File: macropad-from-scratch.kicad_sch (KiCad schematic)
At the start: 0 parts

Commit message: added the MCU, some resistors, and a capacitor
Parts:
- added C1: 1uF, symbol Device:C_Small
- added R1: 10k, symbol Device:R_Small
- added R2, R3: 22, symbol Device:R_Small
- added U3: ATmega32U4-A, Package_QFP:TQFP-44_10x10mm_P0.8mm, symbol MCU_Microchip_ATmega:ATmega32U4-A
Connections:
- new net: R3.2, U3.3 (D-)
- new net: R1.1, U3.33 (~{HWB}/PE2)
- new net: R2.2, U3.4 (D+)
- new net: C1.1, U3.6 (UCAP)
- new net +5V: U3.14 (VCC), U3.2 (UVCC), U3.24 (AVCC), U3.34 (VCC), U3.44 (AVCC)
- new net GND: R1.2, U3.15 (GND), U3.23 (GND), U3.35 (GND), U3.43 (GND), U3.5 (UGND)

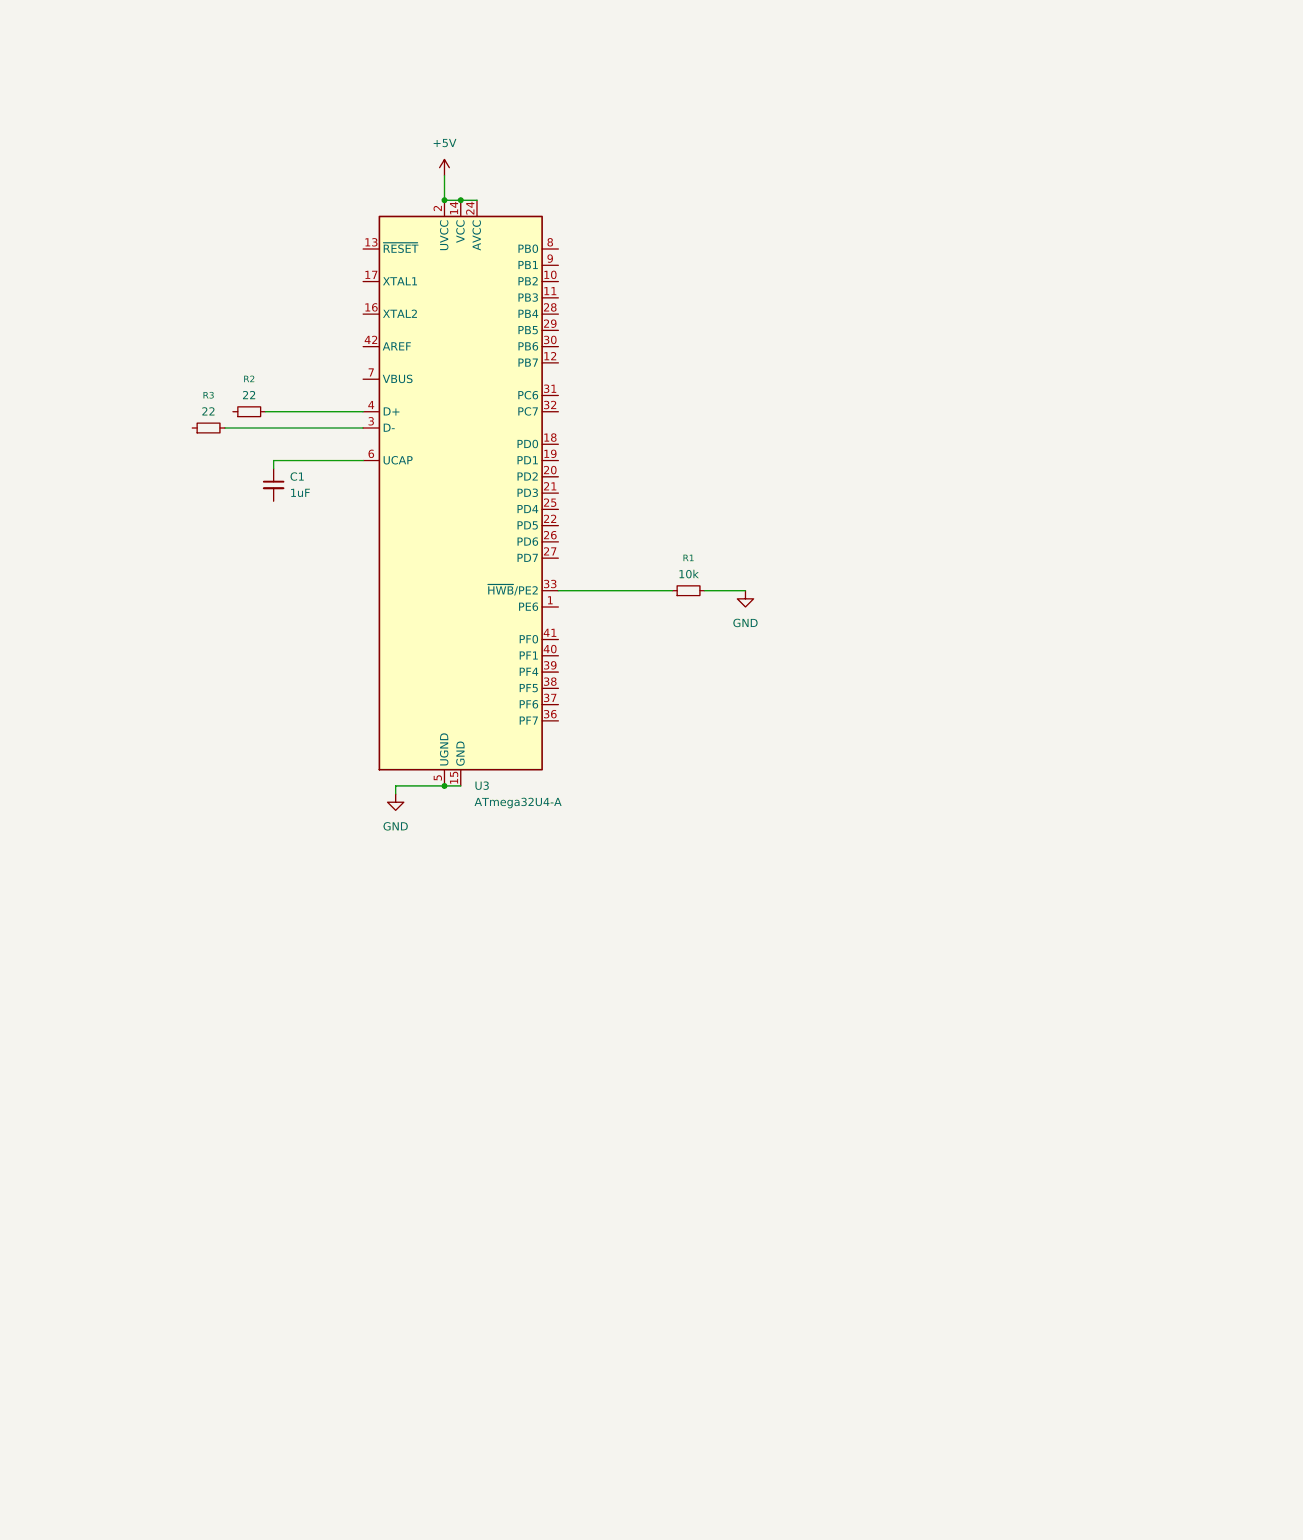
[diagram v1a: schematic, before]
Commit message: Added keyboard matrix
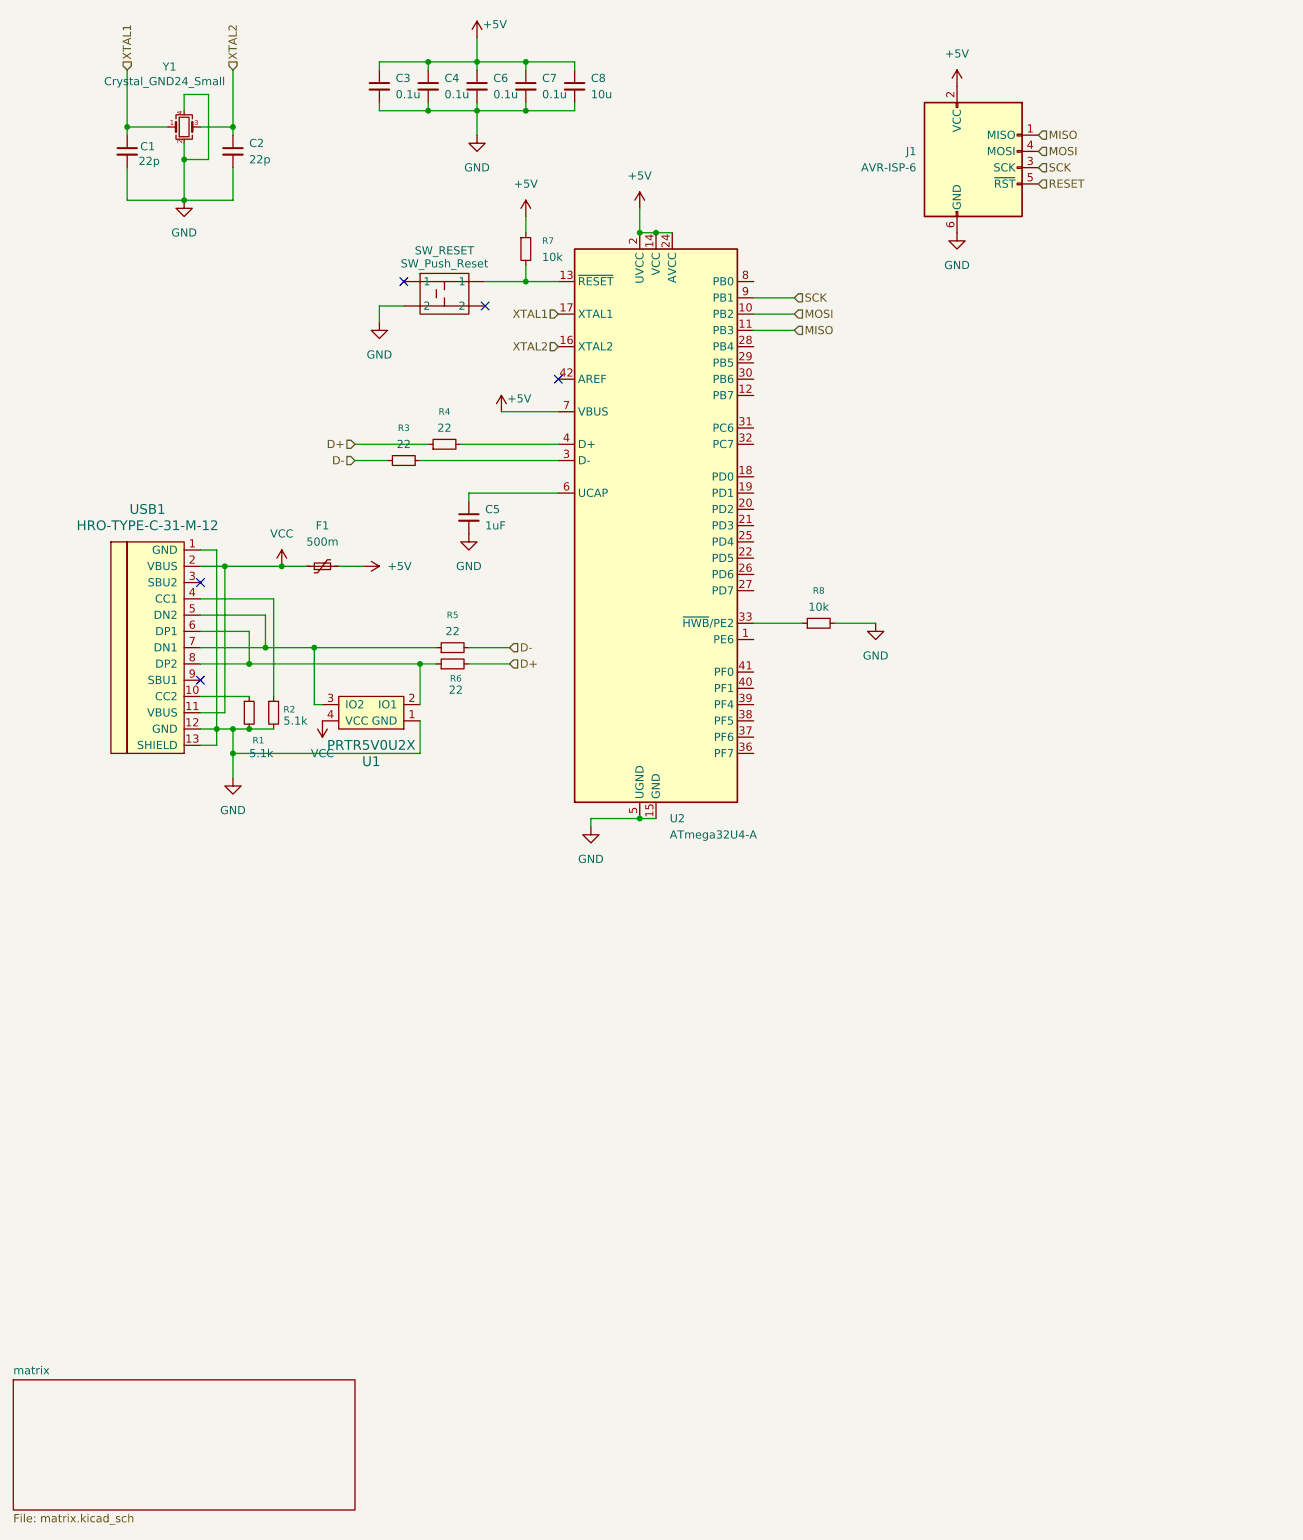
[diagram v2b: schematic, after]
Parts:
- added C1, C2: 22p, symbol Device:C_Small
- added C3, C4, C6, C7: 0.1u, symbol Device:C_Small
- added C8: 10u, symbol Device:C_Small
- added F1: 500m, symbol Device:Polyfuse_Small
- added J1: AVR-ISP-6, symbol Connector:AVR-ISP-6
- added R1, R2: 5.1k, symbol Device:R_Small
- added R5, R6: 22, symbol Device:R_Small
- added R7: 10k, symbol Device:R_Small
- added SW_RESET: SW_Push_Reset, symbol local:SW_PN
- added U1: PRTR5V0U2X, symbol random-keyboard-parts:PRTR5V0U2X
- added USB1: HRO-TYPE-C-31-M-12, symbol Type-C:HRO-TYPE-C-31-M-12
- added Y1: Crystal_GND24_Small, symbol Device:Crystal_GND24_Small
- renumbered C1 to C5, R2 to R4, R1 to R8, U3 to U2
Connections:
- net +5V: now also U2.7 (VBUS), C3.1, C4.1, C6.1, C7.1, C8.1, F1.2, J1.2 (VCC), R7.1
- net GND: now also C5.2, C1.2, C2.2, C3.2, C4.2, C6.2, C7.2, C8.2, J1.6 (GND), R1.2, R2.2, SW_RESET. (2), U1.1 (GND), USB1.1 (GND), USB1.12 (GND), USB1.13 (SHIELD), Y1.2, Y1.4
- net MOSI: now reaches U2.10 (PB2)
- net MOSI: now also J1.4 (MOSI)
- net MISO: now reaches U2.11 (PB3)
- net MISO: now also J1.1 (MISO)
- net at U2.13 (~{RESET}): now also R7.2, SW_RESET. (2)
- net XTAL2: now reaches U2.16 (XTAL2)
- net XTAL2: now also C2.1, Y1.3
- net XTAL1: now reaches U2.17 (XTAL1)
- net XTAL1: now also C1.1, Y1.1
- net SCK: now reaches U2.9 (PB1)
- net SCK: now also J1.3 (SCK)
- net D+: now reaches R4.1
- net D+: now also R6.2
- net D-: now reaches R3.1
- net D-: now also R5.2
- new net: R1.1, USB1.10 (CC2)
- new net: R2.1, USB1.4 (CC1)
- new net: R5.1, U1.3 (IO2), USB1.5 (DN2), USB1.7 (DN1)
- new net: R6.1, U1.2 (IO1), USB1.6 (DP1), USB1.8 (DP2)
- new net RESET: J1.5 (~{RST})
- new net VCC: F1.1, U1.4 (VCC), USB1.11 (VBUS), USB1.2 (VBUS)
- no-connect marks 0 -> 5
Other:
- added sheet matrix (matrix.kicad_sch)
- moved on the sheet: C5, R3, R4, R8, U2

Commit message: completed pcb
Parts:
- removed R5, R6: 22, symbol Device:R_Small
- removed SW_RESET: SW_Push_Reset, symbol local:SW_PN
- added SW85: SW_Push, Button_Switch_SMD:SW_SPST_SKQG_WithStem, symbol Switch:SW_Push
- C1, C2, C3, C4, C6, C7, C8: footprint (none) -> Capacitor_SMD:C_0805_2012Metric_Pad1.18x1.45mm_HandSolder
- C5: value 1uF -> 1u; footprint (none) -> Capacitor_SMD:C_0805_2012Metric_Pad1.18x1.45mm_HandSolder
- F1: footprint (none) -> Fuse:Fuse_1206_3216Metric_Pad1.42x1.75mm_HandSolder
- J1: footprint (none) -> random-keyboard-parts:Reset_Pretty-Mask
- R1, R2, R3, R4, R7, R8: footprint (none) -> Resistor_SMD:R_0805_2012Metric_Pad1.20x1.40mm_HandSolder
- U1: footprint (none) -> random-keyboard-parts:SOT143B
- USB1: footprint (none) -> Type-C:HRO-TYPE-C-31-M-12-HandSoldering
- Y1: footprint (none) -> Crystal:Crystal_SMD_3225-4Pin_3.2x2.5mm_HandSoldering
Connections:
- net D+: now also U1.2 (IO1), USB1.6 (DP1), USB1.8 (DP2)
- net D-: now also U1.3 (IO2), USB1.5 (DN2), USB1.7 (DN1)
- net GND: now also SW85.1
- net RESET: now also R7.2, U2.13 (~{RESET}), SW85.2
- net row0: now reaches U2.1 (PE6)
- net col7: now reaches U2.12 (PB7)
- net col8: now reaches U2.18 (PD0)
- net col9: now reaches U2.19 (PD1)
- net col10: now reaches U2.20 (PD2)
- net col11: now reaches U2.21 (PD3)
- net col12: now reaches U2.22 (PD5)
- net col13: now reaches U2.25 (PD4)
- net col14: now reaches U2.26 (PD6)
- net col15: now reaches U2.27 (PD7)
- net col0: now reaches U2.28 (PB4)
- net col1: now reaches U2.29 (PB5)
- net col2: now reaches U2.30 (PB6)
- net col3: now reaches U2.31 (PC6)
- net col4: now reaches U2.32 (PC7)
- net col5: now reaches U2.36 (PF7)
- net row5: now reaches U2.37 (PF6)
- net row4: now reaches U2.38 (PF5)
- net row3: now reaches U2.39 (PF4)
- net row2: now reaches U2.40 (PF1)
- net row1: now reaches U2.41 (PF0)
- net col6: now reaches U2.8 (PB0)
- no-connect marks 5 -> 4
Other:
- moved on the sheet: C1, C2, C3, C4, C5, C6, C7, C8, F1, J1, R1, R2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
